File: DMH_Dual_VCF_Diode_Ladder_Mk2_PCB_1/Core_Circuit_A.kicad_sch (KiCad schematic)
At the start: 41 parts, among them J19 Conn_01x04_PinHeader, SW1 SW_SPDT, SW2 SW_SPDT, SW3 SW_SPDT, U3 TL074, U5 TL074

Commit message: Corrected pin header footprint assignments
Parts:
- J19: footprint Connector_PinHeader_2.54mm:PinHeader_1x10_P2.54mm_Vertical -> Connector_PinSocket_2.54mm:PinSocket_1x04_P2.54mm_Vertical
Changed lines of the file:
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@@
 			)
 		)
-		(property "Footprint" "Connector_PinHeader_2.54mm:PinHeader_1x10_P2.54mm_Vertical"
+		(property "Footprint" "Connector_PinSocket_2.54mm:PinSocket_1x04_P2.54mm_Vertical"
 			(at 146.05 81.28 0)
 			(effects
@@
 			)
 		)
-		(property "Footprint" "Connector_PinHeader_2.54mm:PinHeader_1x10_P2.54mm_Vertical"
+		(property "Footprint" "Connector_PinSocket_2.54mm:PinSocket_1x04_P2.54mm_Vertical"
 			(at 74.93 41.91 0)
 			(effects
@@
 			)
 		)
-		(property "Footprint" "Connector_PinHeader_2.54mm:PinHeader_1x10_P2.54mm_Vertical"
+		(property "Footprint" "Connector_PinSocket_2.54mm:PinSocket_1x04_P2.54mm_Vertical"
 			(at 134.62 114.3 0)
 			(effects
@@
 			)
 		)
-		(property "Footprint" "Connector_PinHeader_2.54mm:PinHeader_1x10_P2.54mm_Vertical"
+		(property "Footprint" "Connector_PinSocket_2.54mm:PinSocket_1x04_P2.54mm_Vertical"
 			(at 88.9 69.85 0)
 			(effects

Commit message: PCB1 component placement in progress
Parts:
- J19: footprint Connector_PinSocket_2.54mm:PinSocket_1x04_P2.54mm_Vertical -> Connector_PinHeader_2.54mm:PinHeader_1x04_P2.54mm_Vertical
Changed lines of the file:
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@@
 			)
 		)
-		(property "Footprint" "Connector_PinSocket_2.54mm:PinSocket_1x04_P2.54mm_Vertical"
+		(property "Footprint" "Connector_PinHeader_2.54mm:PinHeader_1x04_P2.54mm_Vertical"
 			(at 146.05 81.28 0)
 			(effects
@@
 			)
 		)
-		(property "Footprint" "Connector_PinSocket_2.54mm:PinSocket_1x04_P2.54mm_Vertical"
+		(property "Footprint" "Connector_PinHeader_2.54mm:PinHeader_1x04_P2.54mm_Vertical"
 			(at 74.93 41.91 0)
 			(effects
@@
 			)
 		)
-		(property "Footprint" "Connector_PinSocket_2.54mm:PinSocket_1x04_P2.54mm_Vertical"
+		(property "Footprint" "Connector_PinHeader_2.54mm:PinHeader_1x04_P2.54mm_Vertical"
 			(at 134.62 114.3 0)
 			(effects
@@
 			)
 		)
-		(property "Footprint" "Connector_PinSocket_2.54mm:PinSocket_1x04_P2.54mm_Vertical"
+		(property "Footprint" "Connector_PinHeader_2.54mm:PinHeader_1x04_P2.54mm_Vertical"
 			(at 88.9 69.85 0)
 			(effects

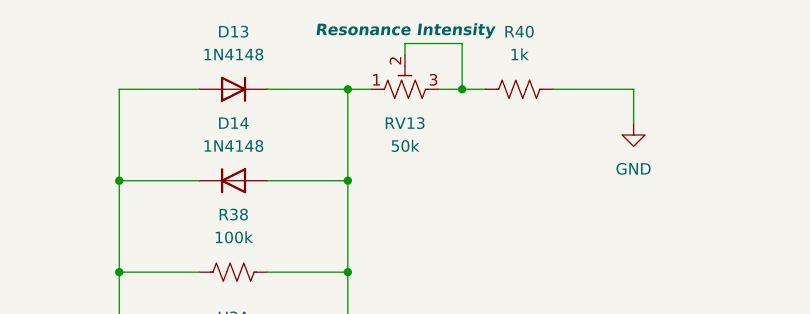
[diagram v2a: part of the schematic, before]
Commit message: Added trim pot functions to silkscreen
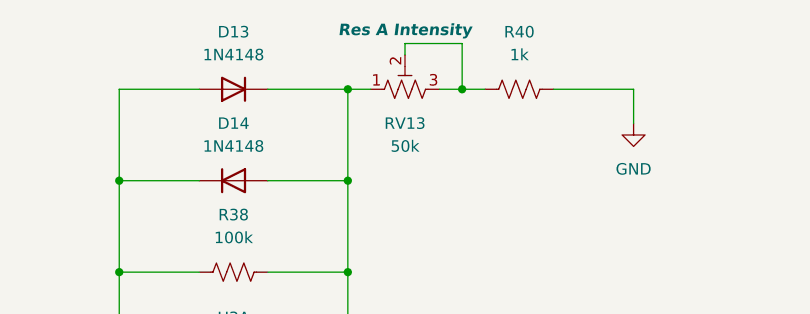
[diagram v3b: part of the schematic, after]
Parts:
- RV13: Function Resonance Intensity -> Res A Intensity
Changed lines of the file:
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@@
 			)
 		)
-		(property "Function" "Resonance Intensity"
+		(property "Function" "Res A Intensity"
 			(at 209.55 23.876 90)
 			(effects

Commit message: validation ongoing
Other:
- note added: "Add 47x gain here for the Resonance VCA. Make following inverter gain unitary."
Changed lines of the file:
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@@
 		(comment 1 "PCB for 15cm Kosmo format synthesizer module")
+	)
+	(rectangle
+		(start 180.34 83.82)
+		(end 204.47 119.38)
+		(stroke
+			(width 0)
+			(type default)
+		)
+		(fill
+			(type none)
+		)
+	)
+	(text "Add 47x gain here for the Resonance VCA.\nMake following inverter gain unitary. "
+		(exclude_from_sim no)
+		(at 202.438 123.698 0)
+		(effects
+			(font
+				(size 1.27 1.27)
+			)
+		)
 	)
 	(junction

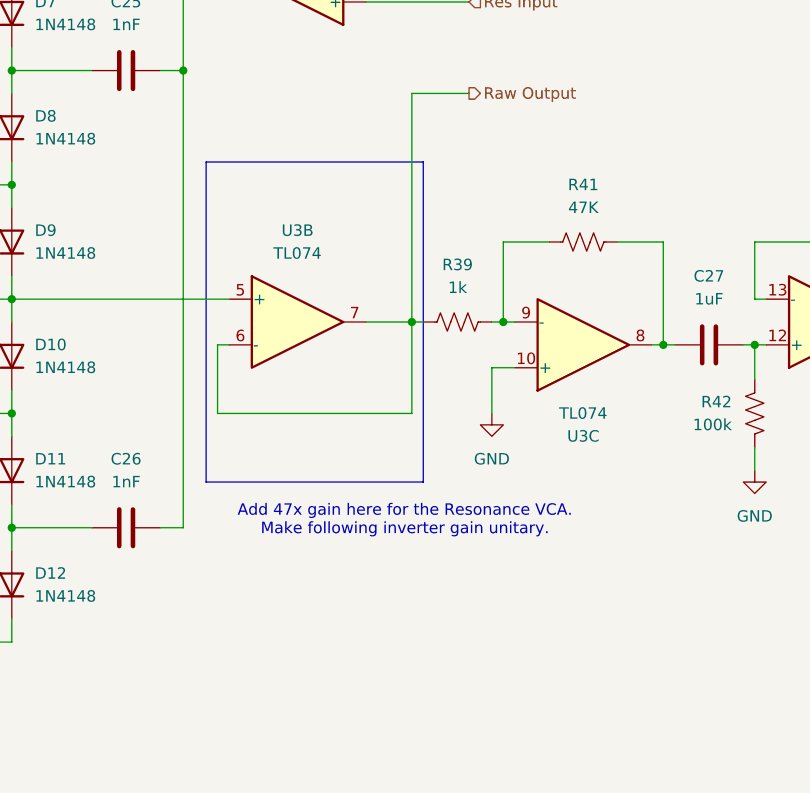
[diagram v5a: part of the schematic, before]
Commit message: Updated schematic during validation
- Changed Resonance B VCA gain resistors to 2k2
- Added range limiting resistors to all Cutoff pots
- Moved 48x gain to non-inverting opamp stage in Core Circuit to allow for Resonance voltage control.
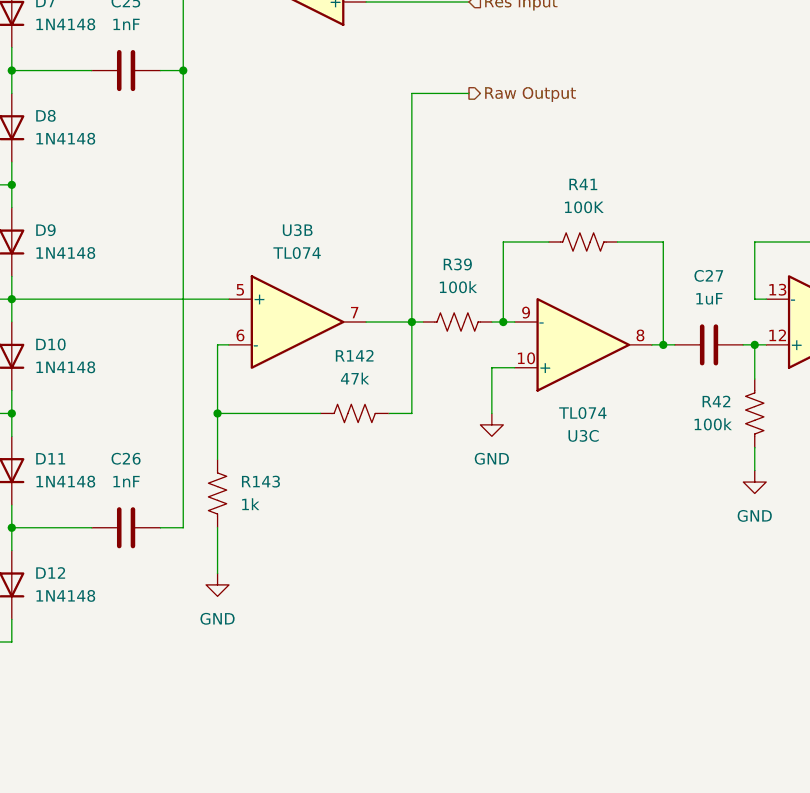
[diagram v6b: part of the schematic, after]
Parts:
- added R142: 47k, Resistor_THT:R_Axial_DIN0207_L6.3mm_D2.5mm_P7.62mm_Horizontal, symbol Device:R_US
- added R143: 1k, Resistor_THT:R_Axial_DIN0207_L6.3mm_D2.5mm_P7.62mm_Horizontal, symbol Device:R_US
- R39: value 1k -> 100k
- R41: value 47K -> 100K
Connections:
- net GND: now also R143.1
- net Raw Output: now also R142.2; no longer U3.6 (-)
- new net: R142.1, R143.2, U3.6 (-)
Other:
- note removed: "Add 47x gain here for the Resonance VCA. Make following inverter gain unitary."
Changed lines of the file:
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@@
 		(comment 1 "PCB for 15cm Kosmo format synthesizer module")
 	)
-	(rectangle
-		(start 180.34 83.82)
-		(end 204.47 119.38)
-		(stroke
-			(width 0)
-			(type default)
-		)
-		(fill
-			(type none)
-		)
-	)
-	(text "Add 47x gain here for the Resonance VCA.\nMake following inverter gain unitary. "
-		(exclude_from_sim no)
-		(at 202.438 123.698 0)
-		(effects
-			(font
-				(size 1.27 1.27)
-			)
-		)
-	)
 	(junction
 		(at 110.49 137.16)
@@
 	)
 	(junction
+		(at 181.61 111.76)
+		(diameter 0)
+		(color 0 0 0 0)
+	)
+	(junction
 		(at 93.98 60.96)
 		(diameter 0)
@@
 	(wire
 		(pts
+			(xy 181.61 111.76) (xy 181.61 116.84)
+		)
+		(stroke
+			(width 0)
+			(type default)
+		)
+	)
+	(wire
+		(pts
 			(xy 78.74 162.56) (xy 78.74 168.91)
 		)
@@
 	(wire
 		(pts
+			(xy 181.61 124.46) (xy 181.61 129.54)
+		)
+		(stroke
+			(width 0)
+			(type default)
+		)
+	)
+	(wire
+		(pts
 			(xy 240.03 104.14) (xy 241.3 104.14)
 		)
@@
 	(wire
 		(pts
-			(xy 181.61 111.76) (xy 203.2 111.76)
+			(xy 181.61 111.76) (xy 193.04 111.76)
 		)
 		(stroke
@@
 	(wire
 		(pts
+			(xy 200.66 111.76) (xy 203.2 111.76)
+		)
+		(stroke
+			(width 0)
+			(type default)
+		)
+	)
+	(wire
+		(pts
 			(xy 25.4 63.5) (xy 31.75 63.5)
 		)
@@
 			)
 		)
-		(property "Value" "47K"
+		(property "Value" "100K"
 			(at 222.25 88.9 90)
 			(effects
@@
 			)
 		)
-		(property "Value" "1k"
+		(property "Value" "100k"
 			(at 208.28 97.79 90)
 			(effects
@@
 	)
 	(symbol
+		(lib_id "Device:R_US")
+		(at 181.61 120.65 180)
+		(unit 1)
+		(exclude_from_sim no)
+		(in_bom yes)
+		(on_board yes)
+		(dnp no)
+		(fields_autoplaced yes)
+		(property "Reference" "R143"
+			(at 184.15 119.3799 0)
+			(effects
+				(font
+					(size 1.27 1.27)
+				)
+				(justify right)
+			)
+		)
+		(property "Value" "1k"
+			(at 184.15 121.9199 0)
+			(effects
+				(font
+					(size 1.27 1.27)
+				)
+				(justify right)
+			)
+		)
+		(property "Footprint" "Resistor_THT:R_Axial_DIN0207_L6.3mm_D2.5mm_P7.62mm_Horizontal"
+			(at 180.594 120.396 90)
+			(effects
+				(font
+					(size 1.27 1.27)
+				)
+				(hide yes)
+			)
+		)
+		(property "Datasheet" "~"
+			(at 181.61 120.65 0)
+			(effects
+				(font
+					(size 1.27 1.27)
+				)
+				(hide yes)
+			)
+		)
+		(property "Description" "Resistor, US symbol"
+			(at 181.61 120.65 0)
+			(effects
+				(font
+					(size 1.27 1.27)
+				)
+				(hide yes)
+			)
+		)
+		(pin "2"
+		)
+		(pin "1"
+		)
+		(instances
+			(project "DMH_Dual_VCF_Diode_Ladder_Mk2_PCB_1"
+				(path "/58f4306d-5387-4983-bb08-41a2313fd315/7ad2d702-dfb7-4d49-a82d-34430dd5948f"
+					(reference "R143")
+					(unit 1)
+				)
+			)
+		)
+	)
+	(symbol
 		(lib_id "Device:C")
 		(at 171.45 124.46 90)
@@
 	(symbol
 		(lib_id "Device:R_US")
+		(at 196.85 111.76 90)
+		(unit 1)
+		(exclude_from_sim no)
+		(in_bom yes)
+		(on_board yes)
+		(dnp no)
+		(fields_autoplaced yes)
+		(property "Reference" "R142"
+			(at 196.85 105.41 90)
+			(effects
+				(font
+					(size 1.27 1.27)
+				)
+			)
+		)
+		(property "Value" "47k"
+			(at 196.85 107.95 90)
+			(effects
+				(font
+					(size 1.27 1.27)
+				)
+			)
+		)
+		(property "Footprint" "Resistor_THT:R_Axial_DIN0207_L6.3mm_D2.5mm_P7.62mm_Horizontal"
+			(at 197.104 110.744 90)
+			(effects
+				(font
+					(size 1.27 1.27)
+				)
+				(hide yes)
+			)
+		)
+		(property "Datasheet" "~"
+			(at 196.85 111.76 0)
+			(effects
+				(font
+					(size 1.27 1.27)
+				)
+				(hide yes)
+			)
+		)
+		(property "Description" "Resistor, US symbol"
+			(at 196.85 111.76 0)
+			(effects
+				(font
+					(size 1.27 1.27)
+				)
+				(hide yes)
+			)
+		)
+		(pin "2"
+		)
+		(pin "1"
+		)
+		(instances
+			(project "DMH_Dual_VCF_Diode_Ladder_Mk2_PCB_1"
+				(path "/58f4306d-5387-4983-bb08-41a2313fd315/7ad2d702-dfb7-4d49-a82d-34430dd5948f"
+					(reference "R142")
+					(unit 1)
+				)
+			)
+		)
+	)
+	(symbol
+		(lib_id "Device:R_US")
 		(at 97.79 162.56 90)
 		(unit 1)
@@
 					(unit 1)
 				)
+			)
+		)
+	)
+	(symbol
+		(lib_id "power:GND")
+		(at 181.61 129.54 0)
+		(unit 1)
+		(exclude_from_sim no)
+		(in_bom yes)
+		(on_board yes)
+		(dnp no)
+		(fields_autoplaced yes)
+		(property "Reference" "#PWR0109"
+			(at 181.61 135.89 0)
+			(effects
+				(font
+					(size 1.27 1.27)
+				)
+				(hide yes)
+			)
+		)
+		(property "Value" "GND"
+			(at 181.61 134.62 0)
+			(effects
+				(font
+					(size 1.27 1.27)
+				)
+			)
+		)
+		(property "Footprint" ""
+			(at 181.61 129.54 0)
+			(effects
+				(font
+					(size 1.27 1.27)
+				)
+				(hide yes)
+			)
+		)
+		(property "Datasheet" ""
+			(at 181.61 129.54 0)
+			(effects
+				(font
+					(size 1.27 1.27)
+				)
+				(hide yes)
+			)
+		)
+		(property "Description" "Power symbol creates a global label with name \"GND\" , ground"
+			(at 181.61 129.54 0)
+			(effects
+				(font
+					(size 1.27 1.27)
+				)
+				(hide yes)
+			)
+		)
+		(pin "1"
+		)
+		(instances
+			(project "DMH_Dual_VCF_Diode_Ladder_Mk2_PCB_1"
+				(path "/58f4306d-5387-4983-bb08-41a2313fd315/7ad2d702-dfb7-4d49-a82d-34430dd5948f"
+					(reference "#PWR0109")
+					(unit 1)
+				)

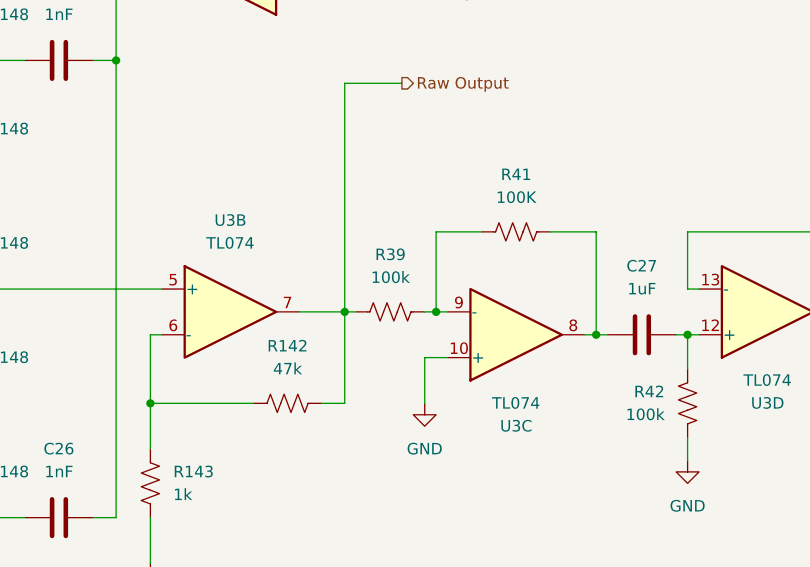
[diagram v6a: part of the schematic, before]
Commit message: Updated various resistor values
... and deleted all VCAs output 1k resistors
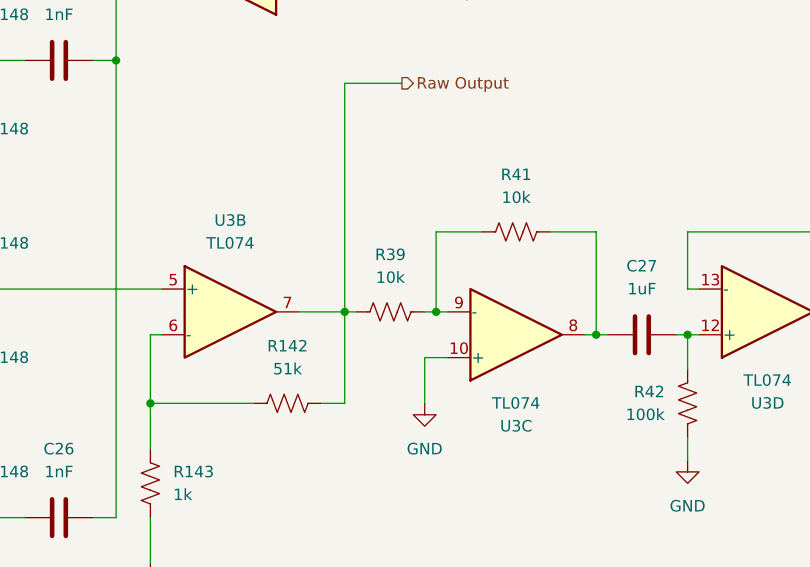
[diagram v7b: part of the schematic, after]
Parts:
- R142: value 47k -> 51k
- R39: value 100k -> 10k
- R41: value 100K -> 10k
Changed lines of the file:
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@@
 			)
 		)
-		(property "Value" "100K"
+		(property "Value" "10k"
 			(at 222.25 88.9 90)
 			(effects
@@
 			)
 		)
-		(property "Value" "100k"
+		(property "Value" "10k"
 			(at 208.28 97.79 90)
 			(effects
@@
 			)
 		)
-		(property "Value" "47k"
+		(property "Value" "51k"
 			(at 196.85 107.95 90)
 			(effects

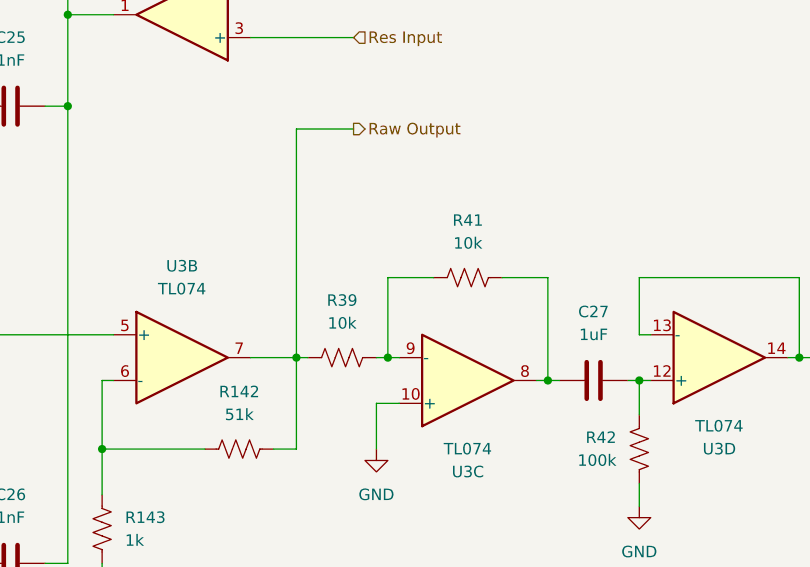
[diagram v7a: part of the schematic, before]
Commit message: Added V/oct calib to CV3 B
And changed output inverter stage resistors back to 100k
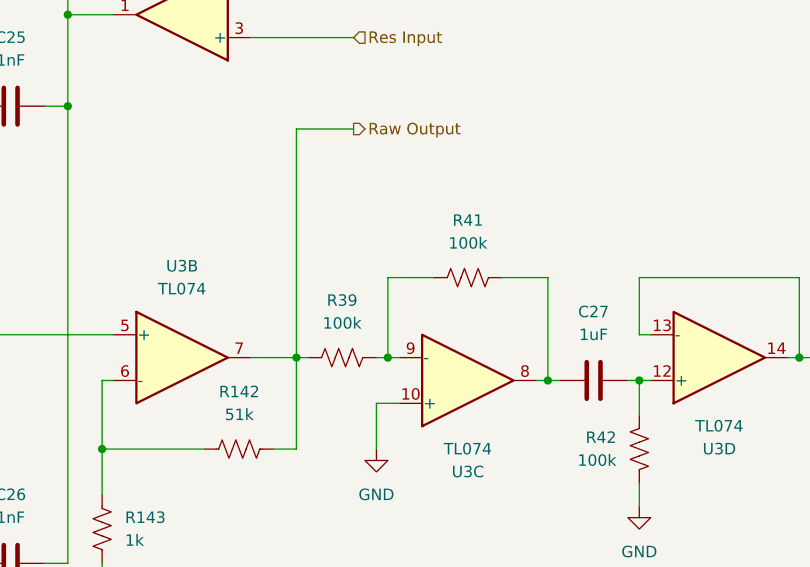
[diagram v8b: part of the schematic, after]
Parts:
- R39, R41: value 10k -> 100k
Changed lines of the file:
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@@
 			)
 		)
-		(property "Value" "10k"
+		(property "Value" "100k"
 			(at 222.25 88.9 90)
 			(effects
@@
 			)
 		)
-		(property "Value" "10k"
+		(property "Value" "100k"
 			(at 208.28 97.79 90)
 			(effects
